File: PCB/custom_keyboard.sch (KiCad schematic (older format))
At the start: 403 parts, among them IC1 FE2.1, J1 USB_A, J2 USB_A, J3 USB_A, J4 Conn_01x08_Male, SW1 SW_Push, U1 PRTR5V0U2X, U2 24LC02, U3 PRTR5V0U2X, U4 PRTR5V0U2X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

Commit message: LED routing
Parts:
- added R54, R55: 20k, Resistor_SMD:R_0805_2012Metric, symbol Device:R_Small
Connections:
- net +5V: now also R54.1, R55.2
- net COL16: now also U9.29 (PD4); no longer U9.30 (PD5)
- net COL17: now also U9.30 (PD5); no longer U9.29 (PD4)
- net ENCODER_A: no longer U9.50 (PA1)
- net ENCODER_B1: now also U9.50 (PA1); no longer U9.49 (PA2)
- net KEYBOARD_SCL: now also R54.2
- net KEYBOARD_SDA: now also R55.1
- net ROT1_ROW: now also U9.59 (PF2); no longer U9.61 (PF0)
- net ROW2: now also U9.61 (PF0); no longer U9.59 (PF2)
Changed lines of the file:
@@
 	1    0    0    -1
 $EndComp
-Text GLabel 9650 19250 1    50   Input ~ 0
+Text GLabel 9550 19250 1    50   Input ~ 0
 KEYBOARD_SDA
 Text GLabel 9800 19250 1    50   Input ~ 0
@@
 L power:+5V #PWR0197
 U 1 1 745E23C2
-P 9500 19250
-F 0 "#PWR0197" H 9500 19100 50  0001 C CNN
-F 1 "+5V" H 9350 19300 50  0000 C CNN
-F 2 "" H 9500 19250 50  0001 C CNN
-F 3 "" H 9500 19250 50  0001 C CNN
-	1    9500 19250
+P 9350 19250
+F 0 "#PWR0197" H 9350 19100 50  0001 C CNN
+F 1 "+5V" H 9200 19300 50  0000 C CNN
+F 2 "" H 9350 19250 50  0001 C CNN
+F 3 "" H 9350 19250 50  0001 C CNN
+	1    9350 19250
 	1    0    0    -1
 $EndComp
@@
 	10000 19350 9800 19350
 Wire Wire Line
-	10000 19500 9650 19500
-Wire Wire Line
-	9500 19650 10000 19650
-Wire Wire Line
 	9350 19800 10000 19800
 Text Notes 9650 18450 0    118  ~ 24
@@
 	9800 19250 9800 19350
 Wire Wire Line
-	9500 19250 9500 19650
+	9350 19250 9350 19350
 Wire Wire Line
-	9650 19500 9650 19250
+	9550 19500 9550 19250
 Wire Wire Line
 	9350 19900 9350 19800
@@
 Wire Wire Line
 	7200 15850 7700 15850
-Text GLabel 7700 18950 2    50   Input ~ 0
-COL17
 Text GLabel 7700 19050 2    50   Input ~ 0
+COL17
+Text GLabel 7700 18950 2    50   Input ~ 0
 COL16
 Text GLabel 7700 19150 2    50   Input ~ 0
@@
 	1    0    0    -1
 $EndComp
-Text GLabel 5650 18550 0    50   Input ~ 0
+Text GLabel 5650 18750 0    50   Input ~ 0
 ROW0
 Text GLabel 5650 18650 0    50   Input ~ 0
 ROW1
-Text GLabel 5650 18750 0    50   Input ~ 0
+Text GLabel 5650 18550 0    50   Input ~ 0
 ROW2
 Text GLabel 5650 18850 0    50   Input ~ 0
@@
 BKL_DATA_IN
 Text GLabel 7700 15950 2    50   Input ~ 0
-ENCODER_A
-Text GLabel 7700 16050 2    50   Input ~ 0
 ENCODER_B1
 Text GLabel 7700 16150 2    50   Input ~ 0
@@
 Text GLabel 7700 17750 2    50   Input ~ 0
 COL4
+Text GLabel 7750 16050 2    50   Input ~ 0
+ENCODER_A
+$Comp
+L Device:R_Small R55
+U 1 1 A0A4D4B3
+P 9450 19500
+F 0 "R55" V 9254 19500 50  0000 C CNN
+F 1 "20k" V 9345 19500 50  0000 C CNN
+F 2 "Resistor_SMD:R_0805_2012Metric" H 9450 19500 50  0001 C CNN
+F 3 "~" H 9450 19500 50  0001 C CNN
+	1    9450 19500
+	0    1    1    0
+$EndComp
+Connection ~ 9550 19500
+Connection ~ 9350 19500
+Wire Wire Line
+	9350 19500 9350 19650
+$Comp
+L Device:R_Small R54
+U 1 1 A0A4DDB4
+P 9700 19350
+F 0 "R54" V 9896 19350 50  0000 C CNN
+F 1 "20k" V 9805 19350 50  0000 C CNN
+F 2 "Resistor_SMD:R_0805_2012Metric" H 9700 19350 50  0001 C CNN
+F 3 "~" H 9700 19350 50  0001 C CNN
+	1    9700 19350
+	0    -1   -1   0
+$EndComp
+Connection ~ 9800 19350
+Wire Wire Line
+	9550 19500 10000 19500
+Wire Wire Line
+	9350 19650 10000 19650
+Wire Wire Line
+	9600 19350 9350 19350
+Connection ~ 9350 19350
+Wire Wire Line
+	9350 19350 9350 19500
 $EndSCHEMATC

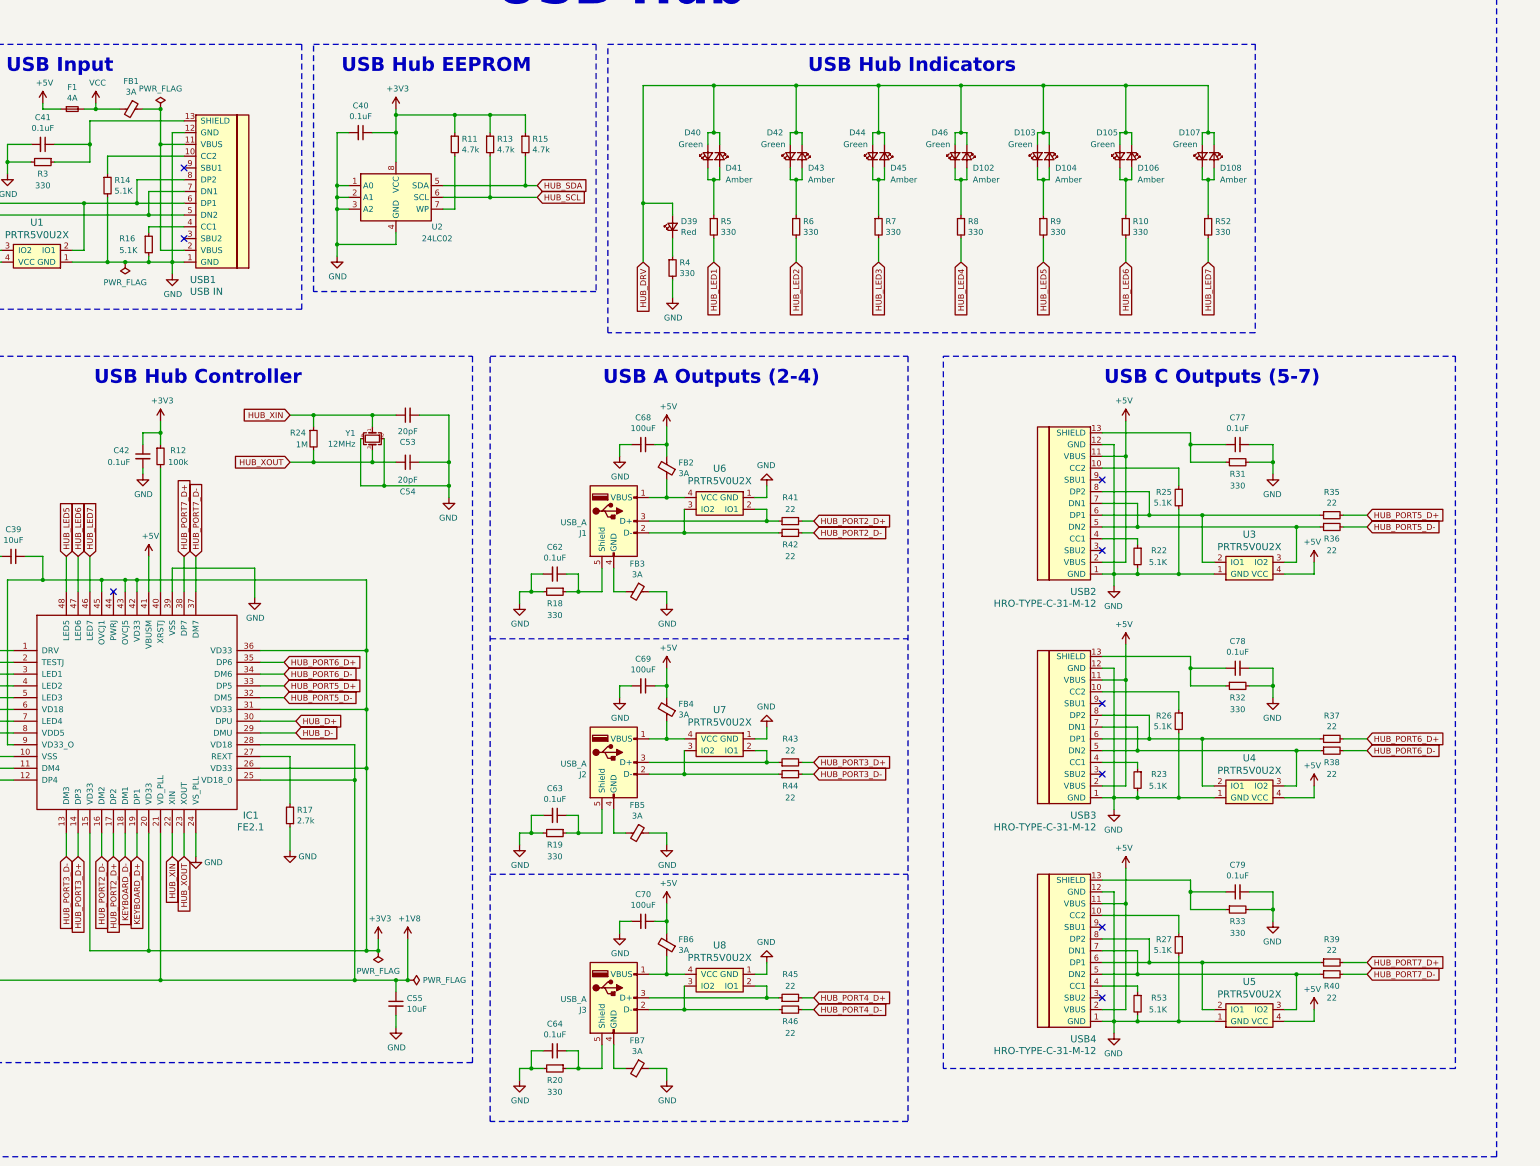
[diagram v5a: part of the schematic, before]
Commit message: LEDs routed, removed 1 USB port
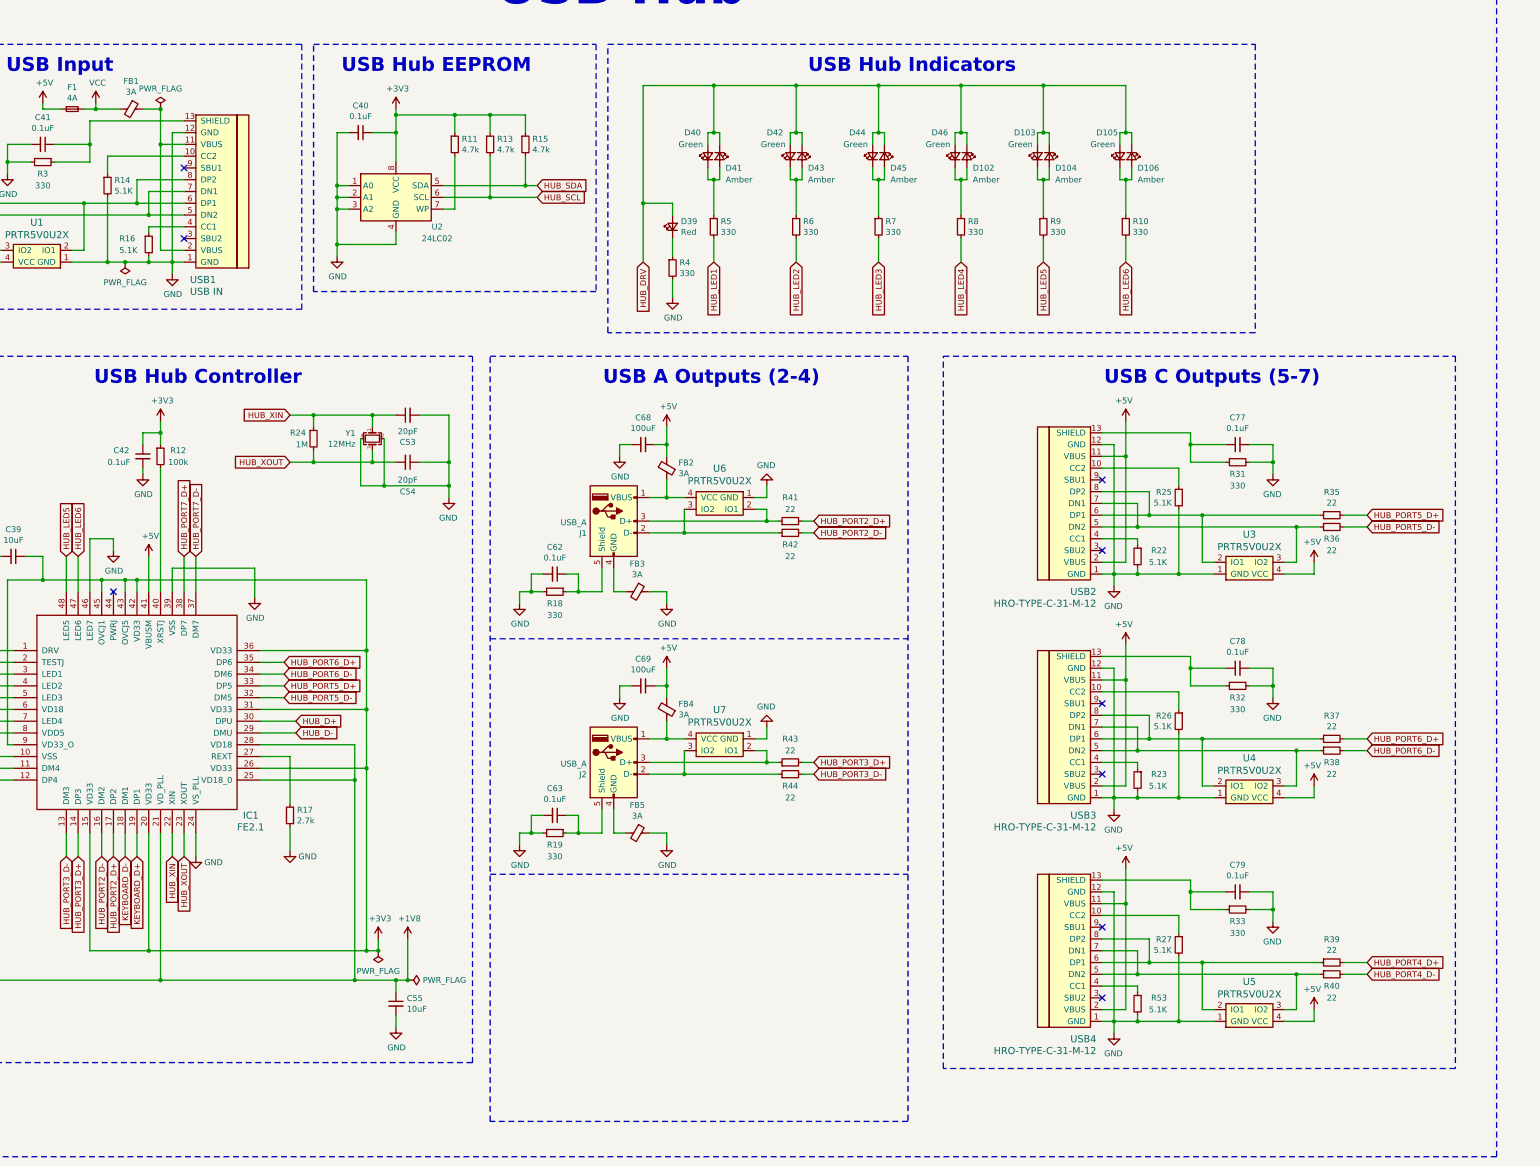
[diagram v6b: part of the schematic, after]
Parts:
- removed C64: 0.1uF, Capacitor_SMD:C_0805_2012Metric, symbol Device:C_Small
- removed C70: 100uF, Capacitor_SMD:C_0805_2012Metric, symbol Device:C_Small
- removed D107: Green, LED_SMD:LED_0402_1005Metric, symbol Device:LED_Small
- removed D108: Amber, LED_SMD:LED_0402_1005Metric, symbol Device:LED_Small
- removed FB6, FB7: 3A, Inductor_SMD:L_0805_2012Metric, symbol Device:Ferrite_Bead_Small
- removed J3: USB_A, random-keyboard-parts:USB-A-Generic, symbol Connector:USB_A
- removed R20, R52: 330, Resistor_SMD:R_0805_2012Metric, symbol Device:R_Small
- removed R45, R46: 22, Resistor_SMD:R_0805_2012Metric, symbol Device:R_Small
- removed U8: PRTR5V0U2X, random-keyboard-parts:SOT143B, symbol random-keyboard-parts:PRTR5V0U2X
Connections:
- net HUB_LED7 is gone; now on net GND: IC1.46 (LED7)
- net HUB_PORT4_D+: now also R39.2
- net HUB_PORT4_D-: now also R40.2
- net HUB_PORT7_D+: no longer R39.2
- net HUB_PORT7_D-: no longer R40.2

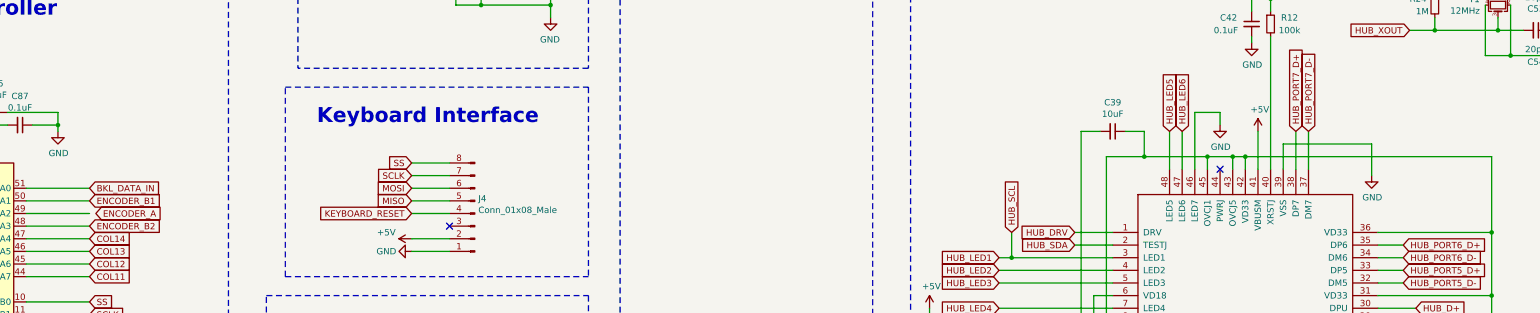
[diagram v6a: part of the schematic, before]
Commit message: Moved USB hub to top, made top gap 0.5u
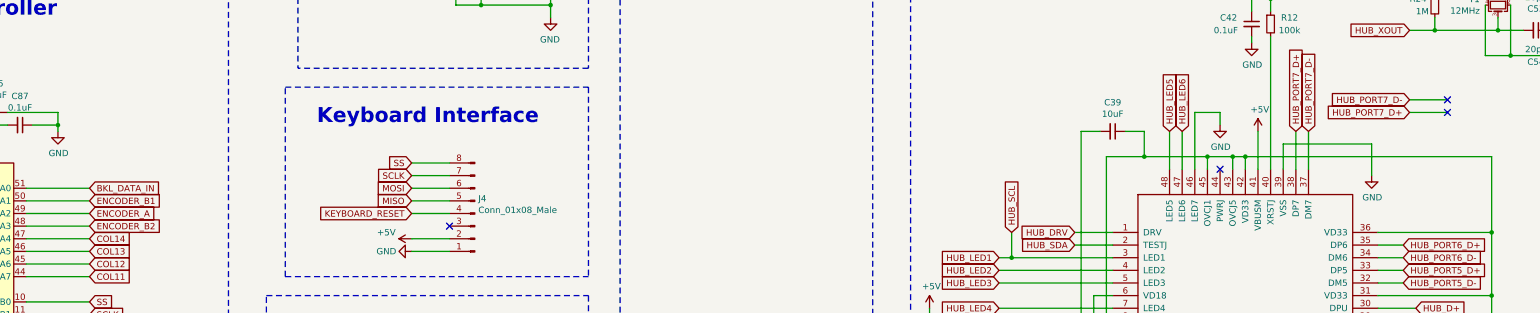
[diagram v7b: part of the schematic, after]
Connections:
- net ENCODER_A: now also U9.49 (PA2)
- no-connect marks 23 -> 25
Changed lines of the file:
@@
 Text GLabel 7700 17750 2    50   Input ~ 0
 COL4
-Text GLabel 7750 16050 2    50   Input ~ 0
+Text GLabel 7700 16050 2    50   Input ~ 0
 ENCODER_A
 $Comp
@@
 HUB_PORT5_D-
 $Comp
-L power:GND #PWR?
+L power:GND #PWR0119
 U 1 1 A66E7532
 P 16650 15350
-F 0 "#PWR?" H 16650 15100 50  0001 C CNN
+F 0 "#PWR0119" H 16650 15100 50  0001 C CNN
 F 1 "GND" H 16655 15177 50  0000 C CNN
 F 2 "" H 16650 15350 50  0001 C CNN
@@
 Wire Wire Line
 	16450 15250 16450 15700
+Text GLabel 18150 15150 0    50   Input ~ 0
+HUB_PORT7_D-
+Text GLabel 18150 15250 0    50   Input ~ 0
+HUB_PORT7_D+
+Wire Wire Line
+	18150 15250 18450 15250
+Wire Wire Line
+	18150 15150 18450 15150
+NoConn ~ 18450 15150
+NoConn ~ 18450 15250
 $EndSCHEMATC

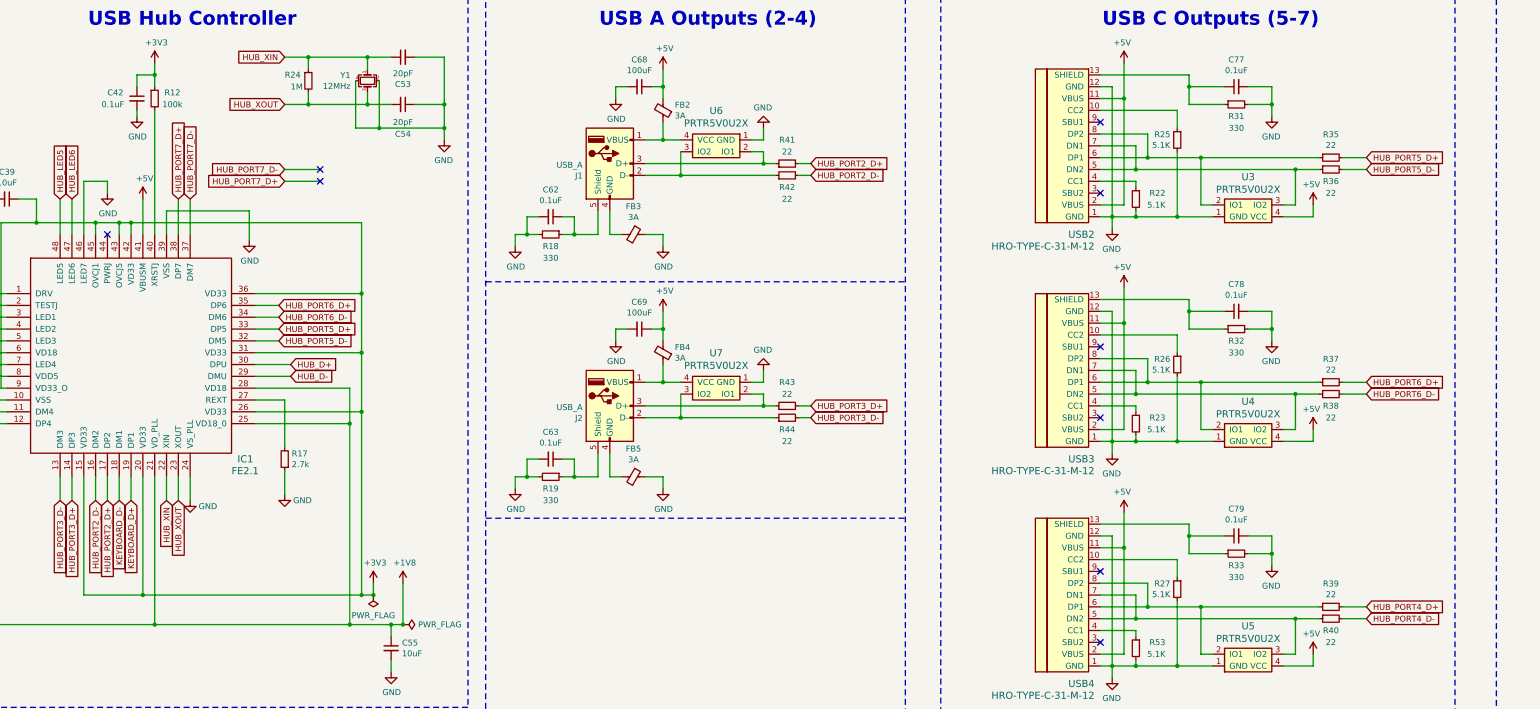
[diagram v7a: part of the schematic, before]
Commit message: Connected all USB ports to hub
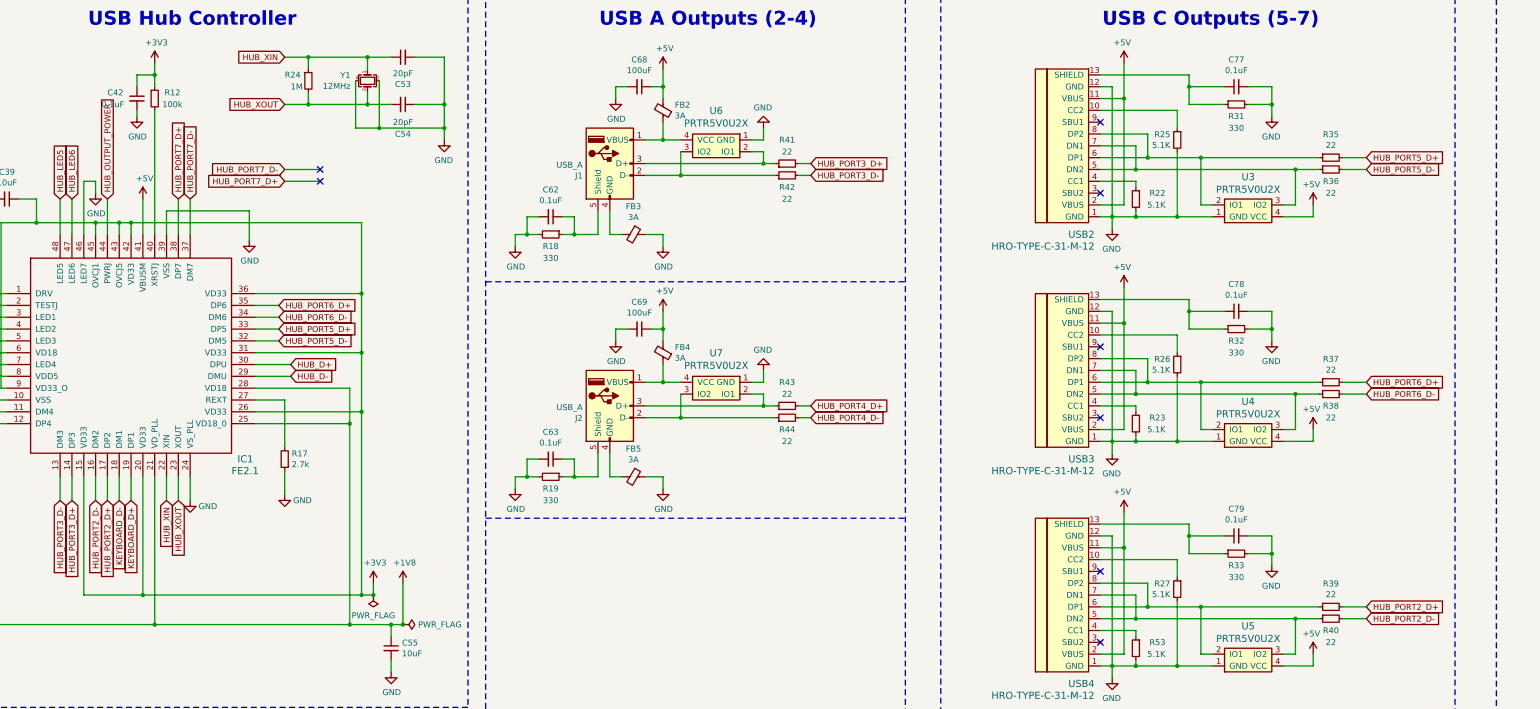
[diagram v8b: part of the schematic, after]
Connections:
- net HUB_PORT2_D+: now also R39.2; no longer R41.2
- net HUB_PORT2_D-: now also R40.2; no longer R42.2
- net HUB_PORT3_D+: now also R41.2; no longer R43.2
- net HUB_PORT3_D-: now also R42.2; no longer R44.2
- net HUB_PORT4_D+: now also R43.2; no longer R39.2
- net HUB_PORT4_D-: now also R44.2; no longer R40.2
- net HUB_OUTPUT_POWER: now reaches IC1.44 (PWRJ)
- no-connect marks 25 -> 24
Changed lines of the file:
@@
 Connection ~ 16850 15600
 Connection ~ 18800 16200
-NoConn ~ 16650 15700
 Wire Wire Line
 	18800 18750 18900 18750
@@
 	0    -1   -1   0
 $EndComp
-Text GLabel 22600 17250 2    50   Input ~ 0
+Text GLabel 22600 15200 2    50   Input ~ 0
 HUB_PORT3_D-
-Text GLabel 22600 17150 2    50   Input ~ 0
+Text GLabel 22600 15100 2    50   Input ~ 0
 HUB_PORT3_D+
 Connection ~ 21350 14450
@@
 	1    0    0    -1
 $EndComp
-Text GLabel 22600 15200 2    50   Input ~ 0
-HUB_PORT2_D-
-Text GLabel 22600 15100 2    50   Input ~ 0
-HUB_PORT2_D+
 $Comp
 L Connector:USB_A J1
@@
 	22200 15100 22300 15100
 Wire Wire Line
-	21200 17150 22200 17150
-Wire Wire Line
-	21200 17250 21500 17250
-Wire Wire Line
-	21500 17050 21500 17250
-Connection ~ 21500 17250
-Wire Wire Line
-	21500 17250 22300 17250
-Wire Wire Line
-	22200 17050 22200 17150
-Connection ~ 22200 17150
-Wire Wire Line
-	22200 17150 22300 17150
-Wire Wire Line
 	21350 14450 21350 14550
 Wire Wire Line
@@
 Wire Wire Line
 	9350 19350 9350 19500
-Text GLabel 27300 18850 2    50   Input ~ 0
-HUB_PORT4_D+
-Text GLabel 27300 18950 2    50   Input ~ 0
-HUB_PORT4_D-
 Text GLabel 27300 17050 2    50   Input ~ 0
 HUB_PORT6_D-
@@
 L power:GND #PWR0119
 U 1 1 A66E7532
-P 16650 15350
-F 0 "#PWR0119" H 16650 15100 50  0001 C CNN
-F 1 "GND" H 16655 15177 50  0000 C CNN
-F 2 "" H 16650 15350 50  0001 C CNN
-F 3 "" H 16650 15350 50  0001 C CNN
-	1    16650 15350
+P 16550 15350
+F 0 "#PWR0119" H 16550 15100 50  0001 C CNN
+F 1 "GND" H 16555 15177 50  0000 C CNN
+F 2 "" H 16550 15350 50  0001 C CNN
+F 3 "" H 16550 15350 50  0001 C CNN
+	1    16550 15350
 	1    0    0    -1
 $EndComp
 Wire Wire Line
-	16450 15250 16650 15250
-Wire Wire Line
-	16650 15250 16650 15350
-Wire Wire Line
 	16450 15250 16450 15700
 Text GLabel 18150 15150 0    50   Input ~ 0
@@
 NoConn ~ 18450 15150
 NoConn ~ 18450 15250
+Text GLabel 16650 15400 1    50   Input ~ 0
+HUB_OUTPUT_POWER
+Wire Wire Line
+	16550 15350 16550 15250
+Wire Wire Line
+	16550 15250 16450 15250
+Wire Wire Line
+	16650 15700 16650 15400
+Text GLabel 22600 17250 2    50   Input ~ 0
+HUB_PORT4_D-
+Text GLabel 22600 17150 2    50   Input ~ 0
+HUB_PORT4_D+
+Text GLabel 27300 18850 2    50   Input ~ 0
+HUB_PORT2_D+
+Text GLabel 27300 18950 2    50   Input ~ 0
+HUB_PORT2_D-
+Wire Wire Line
+	21500 17250 22300 17250
+Wire Wire Line
+	21200 17250 21500 17250
+Connection ~ 21500 17250
+Wire Wire Line
+	21500 17050 21500 17250
+Wire Wire Line
+	22200 17150 22300 17150
+Wire Wire Line
+	21200 17150 22200 17150
+Connection ~ 22200 17150
+Wire Wire Line
+	22200 17050 22200 17150
 $EndSCHEMATC
